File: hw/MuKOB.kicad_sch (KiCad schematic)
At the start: 49 parts, among them J10 Conn_01x04, J11 Conn_01x07, J14 SPKR, J16 Conn_01x30, J17 Conn_02x15_Odd_Even, J3 Micro_SD_Card, J6 Conn_01x03, J7 SER_COM, J8 SJ-43516-SMT-TR, J9 Conn_01x02, Q2 2N3904, SW1 RESET, U1 TLV70033_SOT23-5, U2 PicoW, U3 NC7WZ16P6X, U5 MAX3221

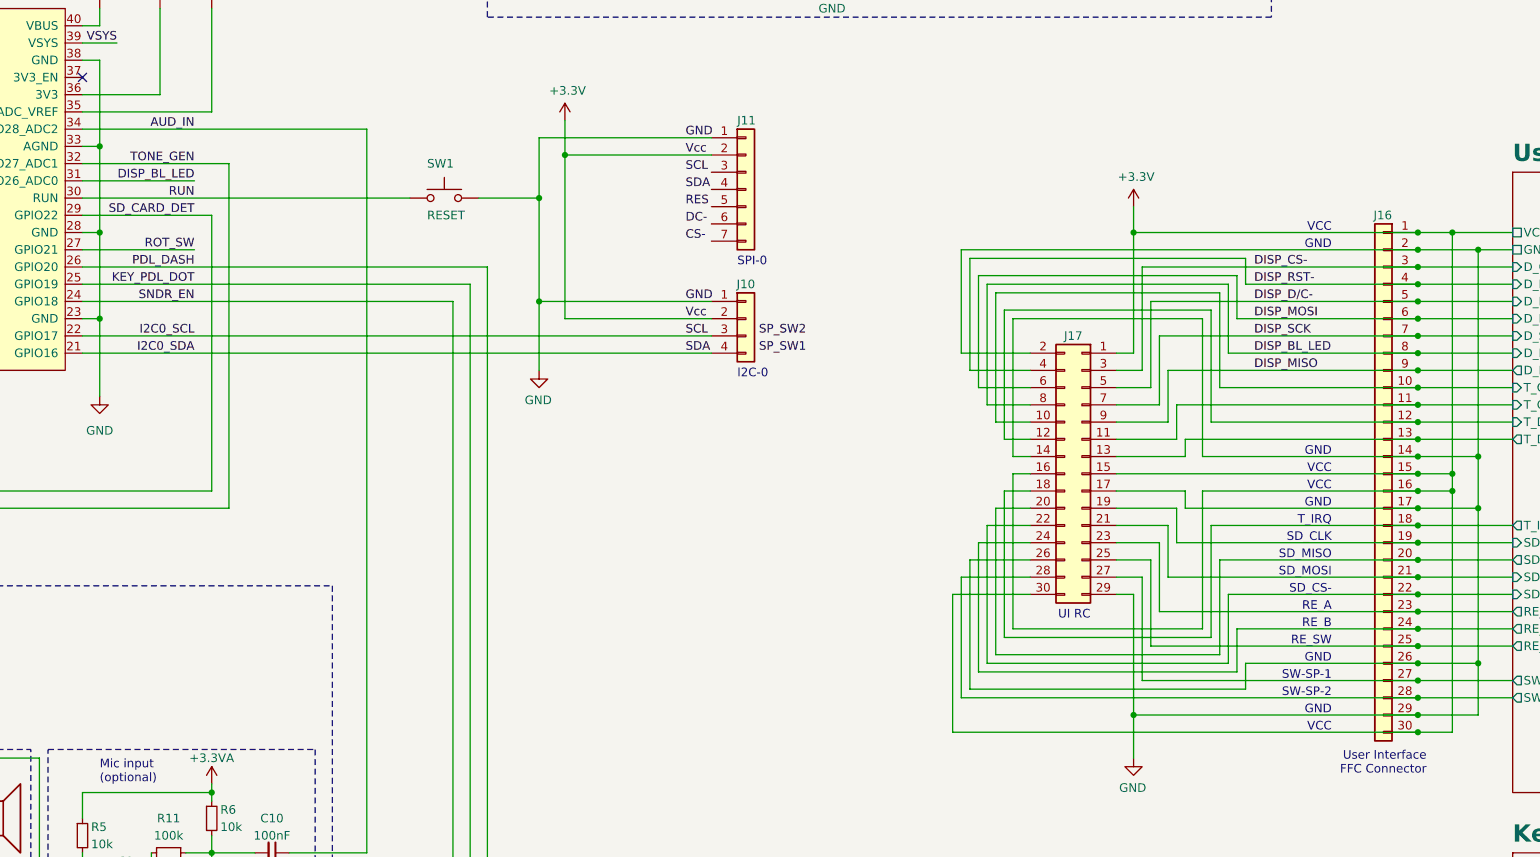
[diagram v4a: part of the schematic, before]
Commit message: Schematic ready for rules check.
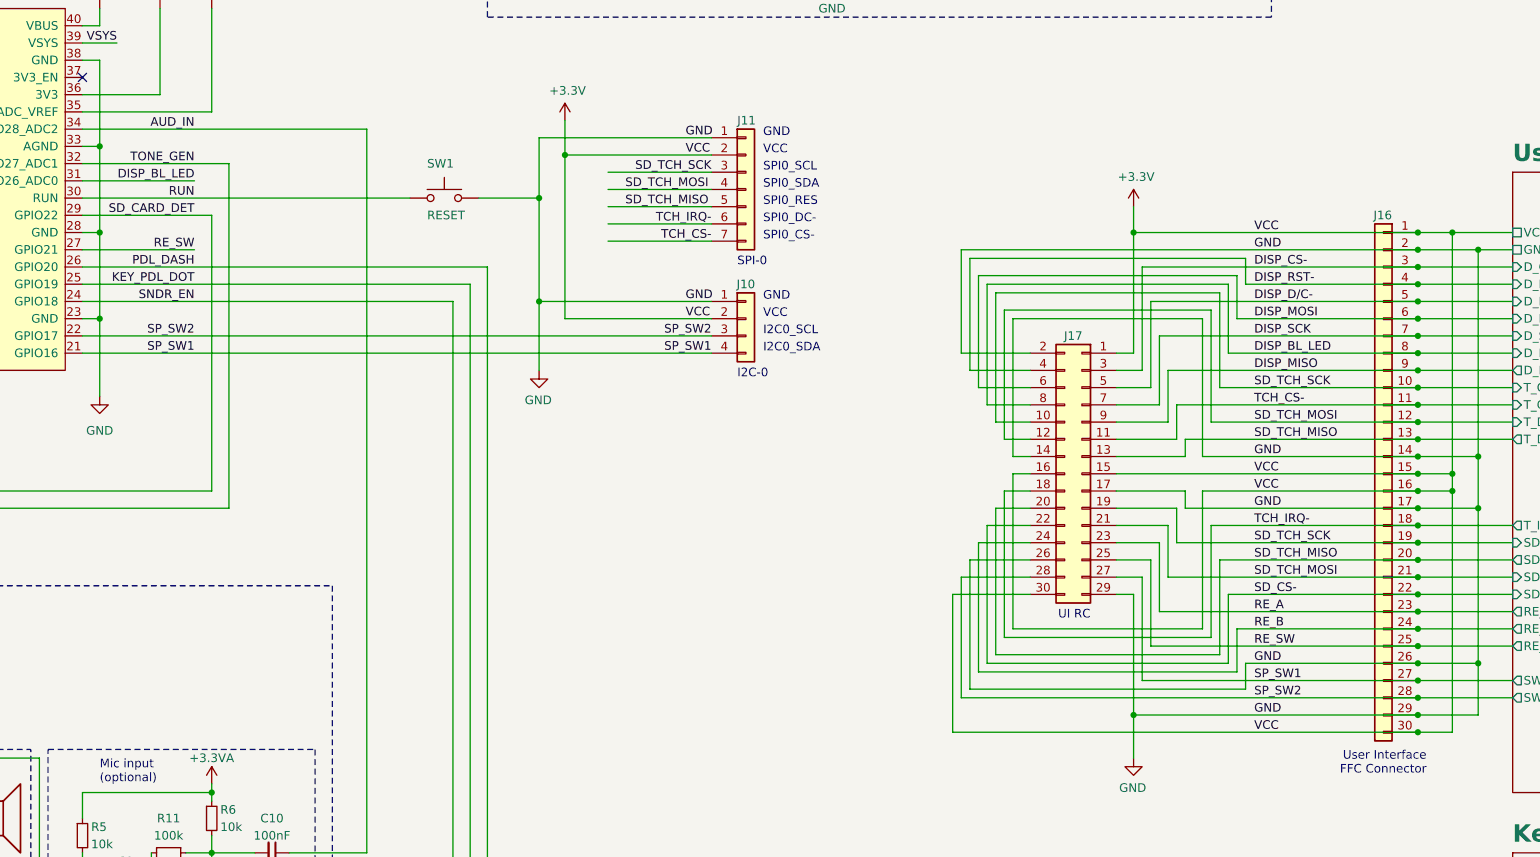
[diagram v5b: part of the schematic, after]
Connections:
- net I2C0_SCL is gone; now on net SP_SW2: J10.3 (Pin_3), U2.22 (GPIO17)
- net I2C0_SDA is gone; now on net SP_SW1: J10.4 (Pin_4), U2.21 (GPIO16)
- net User Interface/RE_A is gone; now on net RE_A: J16.23 (Pin_23), J17.23 (Pin_23)
- net User Interface/RE_B is gone; now on net RE_B: J16.24 (Pin_24), J17.24 (Pin_24)
- net User Interface/RE_SW is gone; now on net RE_SW: J16.25 (Pin_25), J17.25 (Pin_25)
- net User Interface/SD_CLK is gone; now on net SD_CARD_DET: J16.19 (Pin_19), J17.19 (Pin_19)
- net User Interface/SD_CS- is gone; now on net SD_CS-: J16.22 (Pin_22), J17.22 (Pin_22)
- net User Interface/SD_MISO is gone; now on net SD_TCH_MISO: J16.20 (Pin_20), J17.20 (Pin_20)
- net User Interface/SD_MOSI is gone; now on net SD_TCH_MOSI: J16.21 (Pin_21), J17.21 (Pin_21)
- net User Interface/SW-SP-1 is gone; now on net SP_SW1: J16.27 (Pin_27), J17.27 (Pin_27)
- net User Interface/SW-SP-2 is gone; now on net SP_SW2: J16.28 (Pin_28), J17.28 (Pin_28)
- net User Interface/T_CLK is gone; now on net SD_CARD_DET: J16.10 (Pin_10), J17.10 (Pin_10)
- net User Interface/T_CS- is gone; now on net TCH_CS-: J16.11 (Pin_11), J17.11 (Pin_11)
- net User Interface/T_DIN is gone; now on net SD_TCH_MOSI: J16.12 (Pin_12), J17.12 (Pin_12)
- net User Interface/T_DOUT is gone; now on net SD_TCH_MISO: J16.13 (Pin_13), J17.13 (Pin_13)
- net User Interface/T_IRQ is gone; now on net TCH_IRQ-: J16.18 (Pin_18), J17.18 (Pin_18)
- net SD_CARD_DET: now also J11.3 (Pin_3)
- net SD_TCH_MISO: now also J11.5 (Pin_5)
- net SD_TCH_MOSI: now also J11.4 (Pin_4)
- net TCH_CS-: now also J11.7 (Pin_7)
- net TCH_IRQ-: now also J11.6 (Pin_6)
- net ROT_SW renamed RE_SW
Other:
- note added: "I2C0_SCL"
- note added: "I2C0_SDA"
- note added: "SPI0_CS-"
- note added: "SPI0_DC-"
- note added: "SPI0_RES"
- note added: "SPI0_SCL"
- note added: "SPI0_SDA"
- note removed: "RE_A"
- note removed: "RE_B"
- note removed: "RE_SW"
- note removed: "SD_CLK"
- note removed: "SD_CS-"
- note removed: "SD_MISO"
- note removed: "SD_MOSI"
- note removed: "SW-SP-1"
- note removed: "SW-SP-2"
- note removed: "T_IRQ"

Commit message: Change display backlight GPIO.
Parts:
- removed BZ1: Buzzer, symbol Device:Buzzer
- removed C1, C2: 1uF, Capacitor_SMD:C_0603_1608Metric, symbol Device:C
- removed C10, C9: 100nF, symbol Device:C_Small
- removed C14, C15: 47u, Capacitor_SMD:C_0805_2012Metric, symbol Device:C
- removed C4, C7, C8: 100n, Capacitor_SMD:C_0402_1005Metric, symbol Device:C
- removed J14: SPKR, symbol Connector_Generic:Conn_01x02
- removed J8: SJ-43516-SMT-TR, symbol Connector_Audio:AudioJack4_Ground_SwitchTR1
- removed JR1, JR2: 0, Resistor_SMD:R_0000_1005Metric, symbol Device:R
- removed LS1: Speaker, symbol Device:Speaker
- removed Q2: 2N3904, Package_TO_SOT_THT:TO-92_Inline, symbol Transistor_BJT:2N3904
- removed R1, R2: 220, Resistor_SMD:R_0402_1005Metric, symbol Device:R
- removed R11: 100k, symbol Device:R_Small
- removed R3, R4: 100, Resistor_SMD:R_0402_1005Metric, symbol Device:R
- removed R5, R6: 10k, symbol Device:R_Small
- removed R7, R8: 1.8K, Resistor_SMD:R_0402_1005Metric, symbol Device:R
- removed U1: TLV70033_SOT23-5, Package_TO_SOT_SMD:SOT-23-5, symbol Regulator_Linear:TLV70033_SOT23-5
- removed U3: NC7WZ16P6X, Package_TO_SOT_SMD:SOT-363_SC-70-6, symbol RPi_Pico:NC7WZ16P6X
- added OP1, OP2, OP3: OP_A-B, Connector_PinHeader_1.00mm:PinHeader_1x03_P1.00mm_Vertical, symbol MuKOB:Option_A-B
- added TP11, TP7 (x2): Test_Point_01, symbol Test_point_Jump:TP_01
- added U3: MCP23S08-E/SO, SOIC127P1030X265-18N, symbol MuKOB:MCP23S08-E/SO
- J4: renamed from J3; value Micro_SD_Card -> MicroSD-Socket w/Det
- renumbered C11 to C1, C17 to C2, C13 to C3, C12 to C4, C16 to C5, C19 to C6, J7 to J1, J6 to J2, J11 to J5, J10 to J6, J17 to J7, J16 to J8, J9 to JP1, R9 to R1, U5 to U1
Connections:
- net +3V3: now also U3.18 (VDD)
- net AUD_IN: now also U2.31 (GPIO26_ADC0); no longer U2.34 (GPIO28_ADC2)
- net DISP_BL_LED: now also U2.27 (GPIO21); no longer U2.31 (GPIO26_ADC0)
- net DISP_RST-: now also U3.6 (~{RESET})
- net GND: now also J2.1 (Pin_1), U3.4 (A1), U3.5 (A0), U3.9 (VSS); no longer J2.3 (Pin_3), U2.33 (AGND)
- net RE_SW: now also U2.29 (GPIO22); no longer U2.27 (GPIO21)
- net SD_CARD_DET: now also OP1.1 (A), U3.10 (GP0); no longer J4.5 (CLK), J5.3 (Pin_3), J7.10 (Pin_10), J7.19 (Pin_19), J8.10 (Pin_10), J8.19 (Pin_19), R1.2, U2.29 (GPIO22), U2.4 (GPIO2)
- net SD_TCH_MISO: no longer J4.7 (DAT0), U2.6 (GPIO4)
- net SD_TCH_MOSI: no longer J4.3 (CMD), U2.5 (GPIO3)
- net SP_SW1: now also OP2.1 (A), U3.11 (GP1); no longer U2.21 (GPIO16)
- net SP_SW2: now also OP3.1 (A), U3.12 (GP2); no longer U2.22 (GPIO17)
- net UART0_TX: now also J2.3 (Pin_3); no longer J2.1 (Pin_1)
- net TONE_GEN renamed TONE_GEN_L
- new net: OP2.2 (C), U2.21 (GPIO16)
- new net: OP3.2 (C), U2.22 (GPIO17)
- new net: TP7.1 (Pin_1), U3.17 (GP7)
- new net: TP7.1 (Pin_1), U3.16 (GP6)
- new net EX_CS-: OP2.3 (B), U3.7 (~{CS})
- new net EX_IRQ: OP3.3 (B), U3.8 (INT)
- new net GNDA: U2.33 (AGND)
- new net HAS_AUD: TP11.1 (Pin_1), U3.13 (GP3)
- new net SDD_TGR: OP1.2 (C), U2.34 (GPIO28_ADC2)
- new net SD_TCH_SCK: J5.3 (Pin_3), J7.10 (Pin_10), J7.19 (Pin_19), J8.10 (Pin_10), J8.19 (Pin_19)
- new net SD_TP_EX_MISO: J4.7 (DAT0), U2.6 (GPIO4), U3.3 (SO)
- new net SD_TP_EX_MOSI: J4.3 (CMD), U2.5 (GPIO3), U3.2 (SI)
- new net SD_TP_EX_SCK: J4.5 (CLK), R1.2, U2.4 (GPIO2), U3.1 (SCK)
- new net TONE_GEN_R: OP1.3 (B)
- new net VOL_A: U3.14 (GP4)
- new net VOL_B: U3.15 (GP5)
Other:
- removed sheet User Interface
- added sheet Audio (audio.kicad_sch)
- note added: "IO Expansion (Required for full audio+ opt)"
- note added: "Serial Data Comm (Optional)"
- note removed: "3.5mm TRRS Audio (STD)"
- note removed: "Audio Output Option"
- note removed: "Audio Section"
- note removed: "Mic input (optional)"
- note removed: "Needed for Analog out and/or Mic in"
- note removed: "Place JR1+BZ1 or JR2+rest"
- note removed: "Serial Data Comm"
- moved on the sheet: C1, C2, C3, C4, C5, J1, J2, J5, J6, J7, J8, JP1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

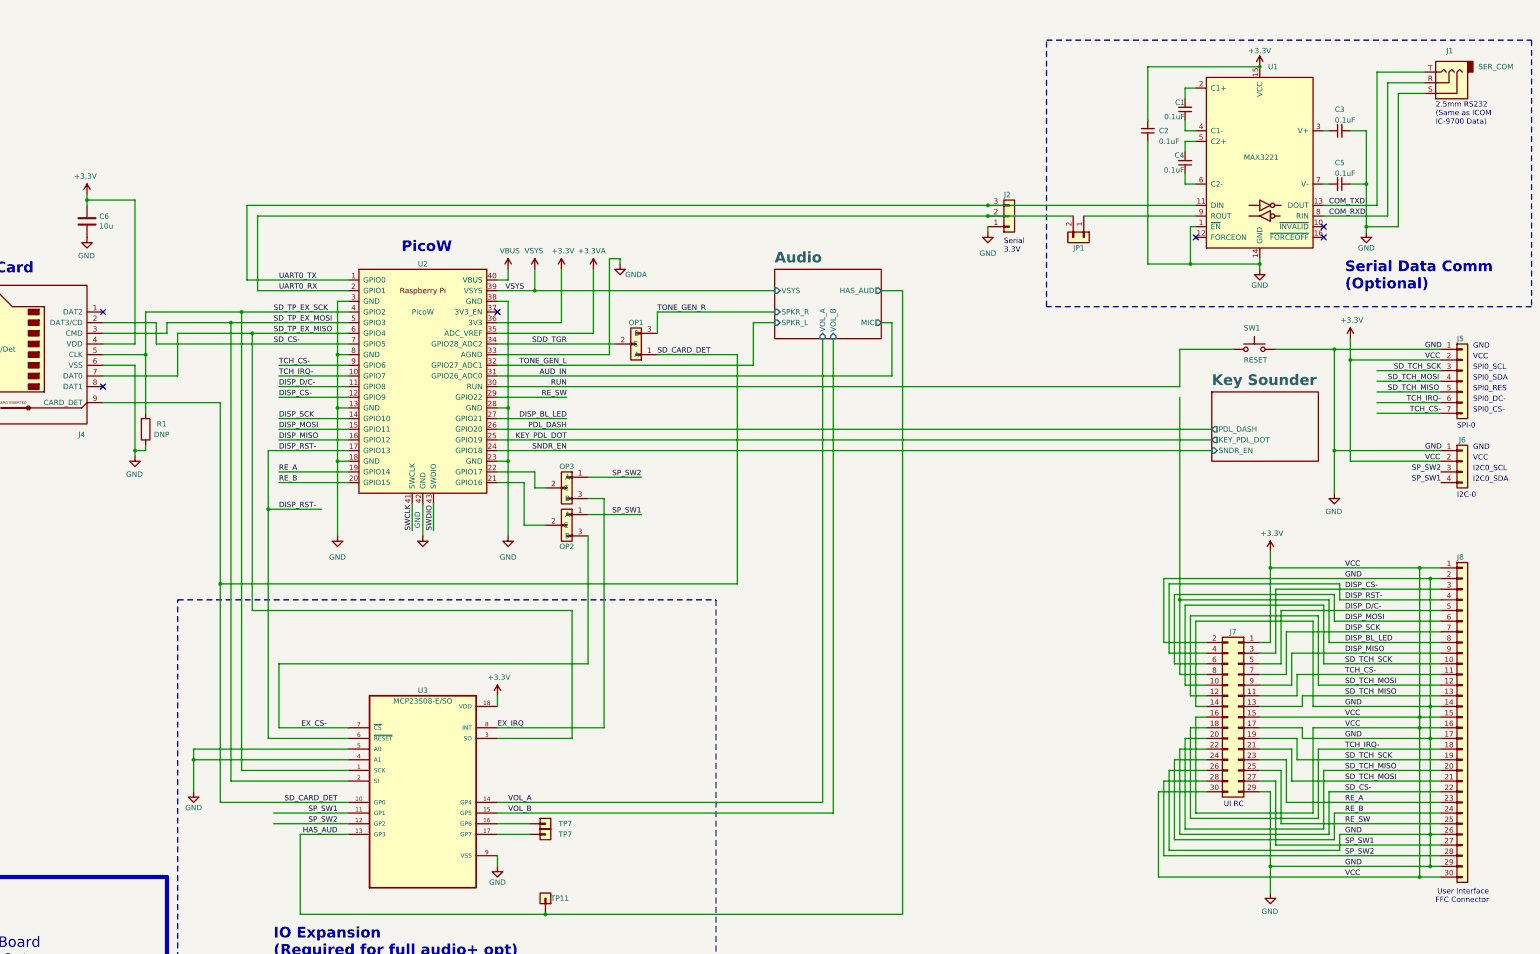
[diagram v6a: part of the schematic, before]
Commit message: Schematic prior to pulling KOB interface to separate board.
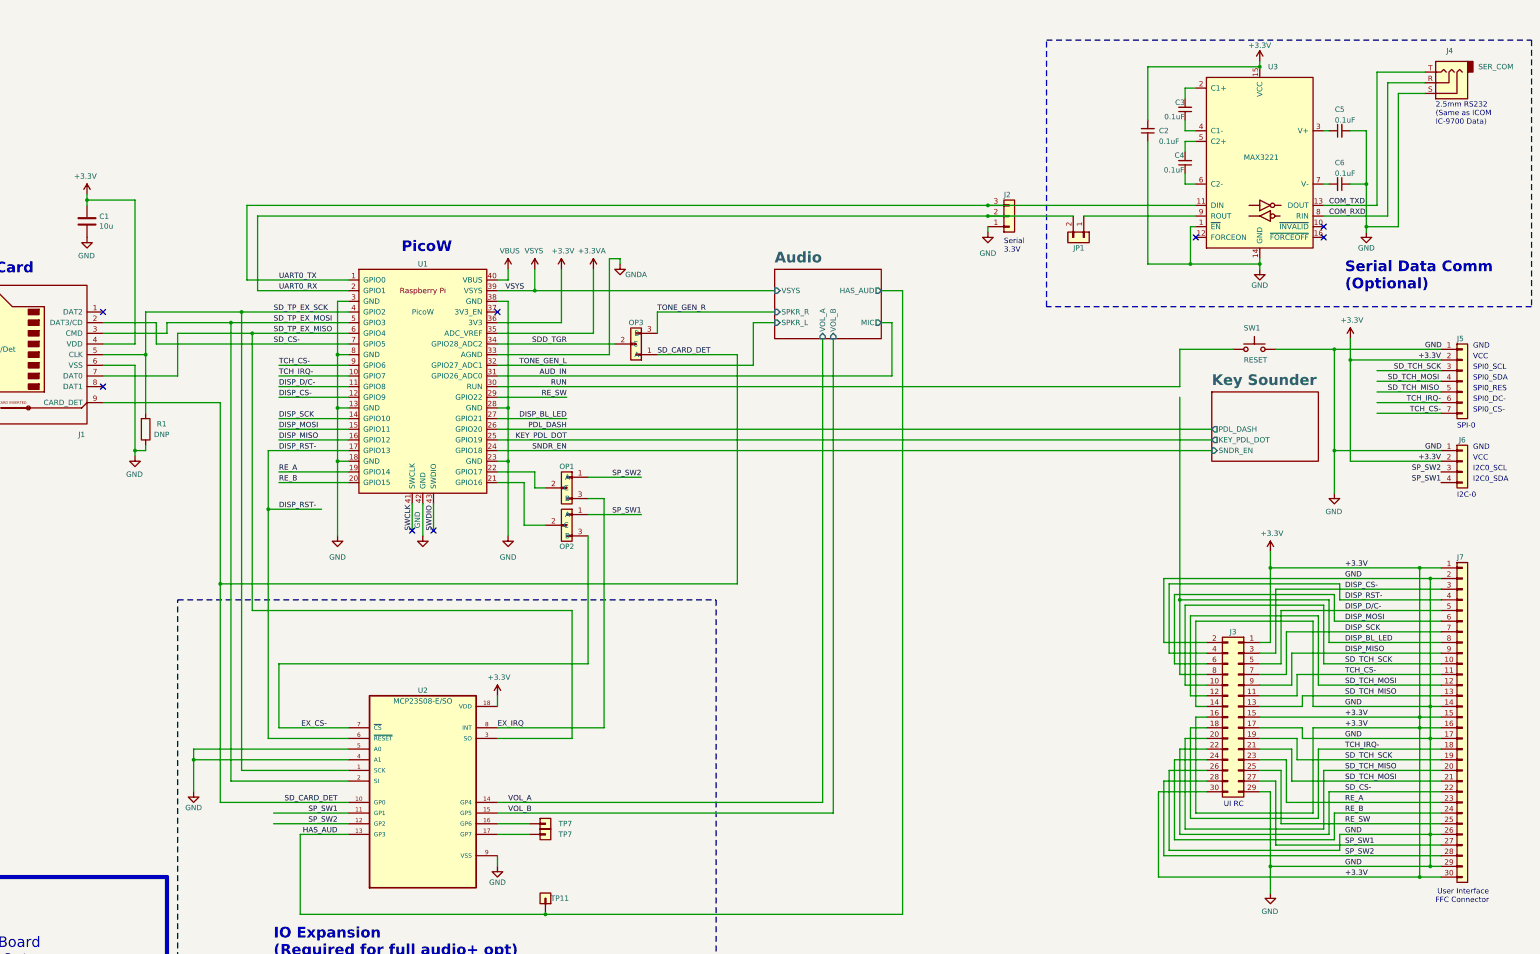
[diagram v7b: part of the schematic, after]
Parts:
- renumbered C6 to C1, C1 to C3, C3 to C5, C5 to C6, J4 to J1, J7 to J3, J1 to J4, J8 to J7, OP3 to OP1, OP1 to OP3, U2 to U1, U3 to U2, U1 to U3
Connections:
- net +3V3 is gone; now on net +3.3V: C1.1, J1.4 (VDD), J3.1 (Pin_1), J3.15 (Pin_15), J3.16 (Pin_16), J3.30 (Pin_30), J5.2 (Pin_2), J6.2 (Pin_2), J7.1 (Pin_1), J7.15 (Pin_15), J7.16 (Pin_16), J7.30 (Pin_30), U1.36 (3V3), U2.18 (VDD)
- no-connect marks 6 -> 8
